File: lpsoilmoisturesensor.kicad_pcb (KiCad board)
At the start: 2 copper layers, 14.7 x 65.2 mm, 7 parts, among them J1 Conn_01x03

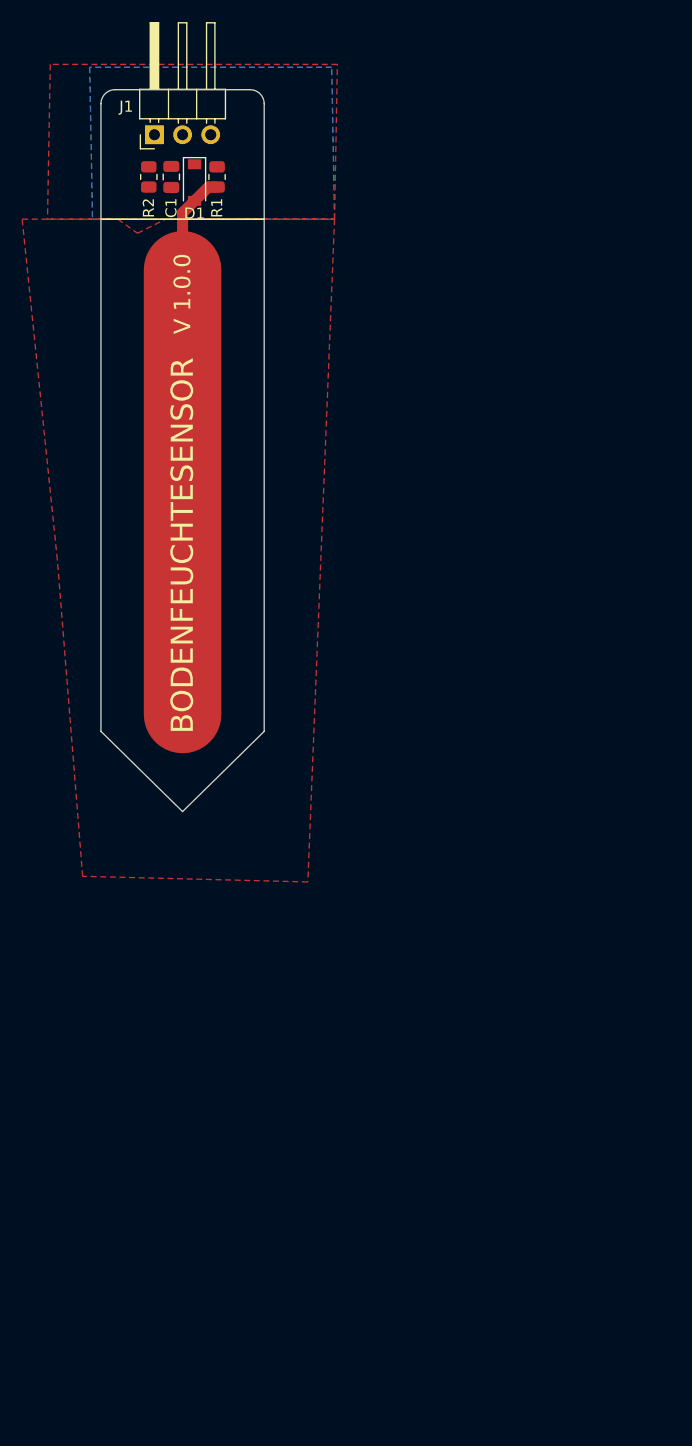
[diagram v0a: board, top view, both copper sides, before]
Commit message: rebuild in kicad v6
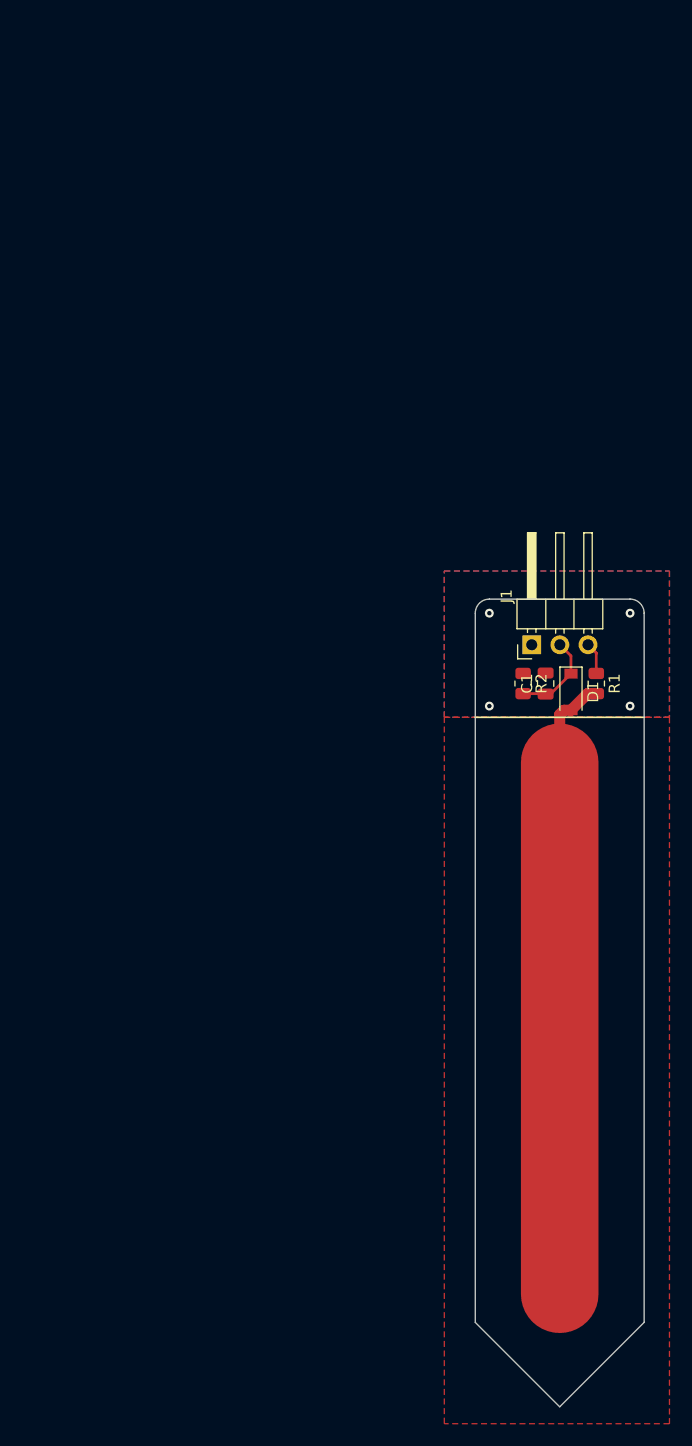
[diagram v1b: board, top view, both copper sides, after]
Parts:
- removed G*** (x2): LOGO, LOGO
- moved J1 57.3 mm to (134.6, 90.7)
- moved D1 57.2 mm to (138.2, 95.0)
- moved R1 57.1 mm to (140.5, 94.2), turned to -90 degrees
- moved R2 56.8 mm to (133.9, 94.2), turned to -90 degrees
- moved C1 56.8 mm to (135.9, 94.2)
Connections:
- C1 pad 1: GND -> /OUT
- C1 pad 2: /OUT -> GND
- D1 pad 2: Net-(D1-A) -> Net-(D1-Pad2)
- R1 pad 1: Net-(D1-A) -> /PULSE
- R1 pad 2: /PULSE -> Net-(D1-Pad2)
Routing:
- net Net-(D1-Pad2): track 0.00 -> 56.4 mm
- net Net-(D1-A): track 49.4 -> 0.00 mm
- net /OUT: track 0.00 -> 8.12 mm
- net /PULSE: track 0.00 -> 2.90 mm
- net GND: vias 0 -> 4
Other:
- board size 14.7 x 65.2 mm -> 15.2 x 72.9 mm
- board text removed: "BODENFEUCHTESENSOR"
- board text removed: "GND"
- board text removed: "OUT"
- board text removed: "PLS"
- board text removed: "V 1.0.0"
- board text removed: "arbeitsgruppe systemsoftware"
